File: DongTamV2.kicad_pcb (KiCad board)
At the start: 2 copper layers, 254 parts, among them J1 KF128, J10 USB_C_Receptacle, J11 KF128, J12 KF128, J13 KF128, J14 Screw_Terminal_01x08, J15 Screw_Terminal_01x08, J16 Screw_Terminal_01x08, J17 Screw_Terminal_01x08, J2 KF128, J3 Conn_01x02_Male, J4 Conn_02x03_Odd_Even, J5 Conn_01x05_Male, J6 Conn_01x04_Male, J7 Conn_01x05_Male, J8 Conn_01x05_Male, J9 IDC_02x07, Q1 N_Mosfet, Q10 SI2302, Q11 SI2302, Q12 SI2302, Q13 SI2302, Q14 SI2302, Q15 SI2302, Q16 SI2302, Q17 SI2302, Q18 SI2302, Q19 SI2302, Q2 N_Mosfet, Q20 SI2302, Q21 SI2302, Q3 N_Mosfet, Q4 N_Mosfet, Q5 N_Mosfet, Q6 SI2302, Q7 SI2302, Q8 SI2302, Q9 SI2302, SW1 PTS810, SW2 PTS810, SW3 PTS810, U1 AM22-24W2405V, U10 LD1117, U11 LM324, U12 LM324, U13 LM324, U14 LM324, U15 MCP41010, U16 74HC165, U17 74HC165, U2 SP3485EN, U3 MCU_STM32F103C8Tx, U4 ESP32-WROOM-32, U5 PCF8563TS, U6 AMS5915, U7 74HC595, U8 74HC595, U9 USBLC6-2SC6, Y1 16MHz, Y2 MC-306

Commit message: finish some unconnect pins, draw edge cut board
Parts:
- added H1: MountingHole, MountingHole:MountingHole_3.2mm_M3, F.Cu at (0.00, 0.00)
- added H2: MountingHole, MountingHole:MountingHole_3.2mm_M3, F.Cu at (0.00, 74.5)
- added H3: MountingHole, MountingHole:MountingHole_3.2mm_M3, F.Cu at (246.8, 0.00)
- added H4: MountingHole, MountingHole:MountingHole_3.2mm_M3, F.Cu at (246.8, 74.9)
- added RV2: TC33X_10k, SpiritBoi_Footprint_Library:Potentiometer-Vert-SMD-3P-Bourns_TC33X, F.Cu at (182.8, 44.5)
- D1, D2, D3: value D_TVS -> SMAJ28A
- F1: value Fuse -> 5x20mm 2A
- F2, F3: value Polyfuse -> MF-MSMF050-2
- FL1: value Filter_EMI_LL -> UU9.8-153 15mH
- J14, J15, J16, J17: value Screw_Terminal_01x08 -> KF-5.08-8-V
- Q1, Q2, Q3, Q4, Q5: value N_Mosfet -> SI2302/BSS138
- RV1: value Varistor -> 14D471K
- moved J13 200.1 mm to (10.5, 92.5)
- moved J11 171.2 mm to (39.0, 93.0)
- moved Y1 169.1 mm to (161.5, 5.00)
- moved C10 165.9 mm to (145.2, 12.8)
- moved C11 165.9 mm to (145.2, 15.4)
- moved C12 165.9 mm to (145.2, 18.1)
- moved C9 165.9 mm to (145.2, 10.2)
- moved JP3 165.9 mm to (149.4, 9.75)
- moved LE1 165.9 mm to (153.9, 6.65)
- moved SW1 165.9 mm to (150.7, 14.0)
- moved C5 162.6 mm to (133.0, -9.50)
- moved J12 160.2 mm to (50.0, 92.0)
- moved R10 160.1 mm to (139.5, 16.9)
- moved R11 160.1 mm to (139.5, 19.5)
- moved R12 160.1 mm to (139.5, 22.1)
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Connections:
- R1 pad 1: /RS485/RS485.TX -> /RS485/RS485_input.TX
- R2 pad 1: /RS485/RS485.RX -> /RS485/RS485_input.RX
- U16 pad 1: /ReadValveState/74HC165.LOAD -> /ReadValveState/InputExpanderPort.LOAD
- U16 pad 2: /ReadValveState/74HC165.SCK -> /ReadValveState/InputExpanderPort.SCK
- U16 pad 9: /ReadValveState/74HC165.DATA -> /ReadValveState/InputExpanderPort.DATA
- U17 pad 1: /ReadValveState/74HC165.LOAD -> /ReadValveState/InputExpanderPort.LOAD
- U17 pad 2: /ReadValveState/74HC165.SCK -> /ReadValveState/InputExpanderPort.SCK
- U2 pad 2: /RS485/RS485.DERE -> /RS485/RS485_input.DERE
- U2 pad 3: /RS485/RS485.DERE -> /RS485/RS485_input.DERE
- U3 pad 1: /STM32/VBAT -> +3.3V
- U4 pad 4: /ESP32/BT.s4 -> /ESP32/GUI_Button.s3
- U4 pad 5: /ESP32/BT.s3 -> /ESP32/GUI_Button.s4
- U4 pad 6: /ESP32/BT.s2 -> /ESP32/GUI_Button.s1
- U4 pad 7: /ESP32/BT.s1 -> /ESP32/GUI_Button.s2
- U5 pad 5: /PCF8563/i2c.SDA -> /AMS5915/i2c.SDA
- U5 pad 6: /PCF8563/i2c.SCL -> /AMS5915/i2c.SCL
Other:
- board outline added: 254 x 125.5 mm
- board text added: "Còn Lora, thẻ nhớ, mạch đọc 4-20mA"

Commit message: Add LORA, SDcard and Volt to 4_20mA scheamtic
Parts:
- removed the J5 at (161.0, 12.0)
- removed the J6 at (160.0, 33.5)
- removed JP3, JP4, JP6: SolderJumper_2_Open, Jumper:SolderJumper-2_P1.3mm_Open_RoundedPad1.0x1.5mm
- added C38: 100nF, SpiritBoi_Footprint_Library:C_0603, F.Cu at (82.5, 15.0)
- added C39: 100nF, SpiritBoi_Footprint_Library:C_0603, F.Cu at (-12.4, 37.0)
- added C41: 100nF, SpiritBoi_Footprint_Library:C_0805, F.Cu at (-36.8, 45.3)
- added D25: SMF05C, SpiritBoi_Footprint_Library:Package-IC-TSSOP_6, F.Cu at (74.5, -1.20)
- added D26: SS54, SpiritBoi_Footprint_Library:Package-Diode-D_SMA, F.Cu at (-13.7, 20.0)
- added J17: Micro_SD_Card_Det1, SpiritBoi_Footprint_Library:Socket_MicroSD-9P, F.Cu at (85.2, 8.68)
- added J18: HT3.96mm-3P, SpiritBoi_Footprint_Library:TerminalBlock_bornier-3_P5.08mm, F.Cu at (-23.4, 27.9)
- added J8: ~, SpiritBoi_Footprint_Library:Conn-Vert-THT-2.54mm-2x4P-IDC_Header, F.Cu at (145.5, 25.0)
- added LE19: Blue 0603, SpiritBoi_Footprint_Library:LED_0603, F.Cu at (-12.2, 39.7)
- added LE20: LED 0805, SpiritBoi_Footprint_Library:LED_0805, F.Cu at (-11.9, 34.1)
- added Q22: MMBT3904, SpiritBoi_Footprint_Library:SOT23-3, F.Cu at (-15.6, 15.4)
- added R102: 4k7, SpiritBoi_Footprint_Library:R_0603, F.Cu at (78.3, 15.0)
- added R103: 220R, SpiritBoi_Footprint_Library:R_0603, F.Cu at (-37.0, 14.3)
- added R104: 1k, SpiritBoi_Footprint_Library:R_0603, F.Cu at (-37.0, 16.9)
- added R105: 10k, SpiritBoi_Footprint_Library:R_0603, F.Cu at (-37.0, 19.6)
- added R106: 560R, SpiritBoi_Footprint_Library:R_0603, F.Cu at (-37.0, 22.2)
- added R107: 100k, SpiritBoi_Footprint_Library:R_0603, F.Cu at (-37.0, 24.9)
- added R108: 100k, SpiritBoi_Footprint_Library:R_0603, F.Cu at (-37.0, 27.5)
- added R109: 820k, SpiritBoi_Footprint_Library:R_0603, F.Cu at (-32.9, 14.3)
- added R110: 820k, SpiritBoi_Footprint_Library:R_0603, F.Cu at (-32.9, 16.9)
- added R111: 820k, SpiritBoi_Footprint_Library:R_0603, F.Cu at (-32.9, 19.6)
- added R112: 820k, SpiritBoi_Footprint_Library:R_0603, F.Cu at (-32.9, 22.2)
- added R113: 820k, SpiritBoi_Footprint_Library:R_0603, F.Cu at (-32.9, 24.9)
- added R114: 820k, SpiritBoi_Footprint_Library:R_0603, F.Cu at (-32.9, 27.5)
- added R115: 100R, SpiritBoi_Footprint_Library:R_0603, F.Cu at (-28.8, 14.3)
- added R116: 680k, SpiritBoi_Footprint_Library:R_0603, F.Cu at (-28.8, 16.9)
- added R117: 820k, SpiritBoi_Footprint_Library:R_0603, F.Cu at (-28.8, 19.6)
- added RV3: 100k, SpiritBoi_Footprint_Library:Potentiometer-Vert-THT-Bourns_3296W, F.Cu at (-31.0, 32.1)
- added RV4: 100k, SpiritBoi_Footprint_Library:Potentiometer-Vert-THT-Bourns_3296W, F.Cu at (-31.0, 38.5)
- added U17: RF_Module_Ai-Thinker-Ra-02, SpiritBoi_Footprint_Library:Module-LORA-RA02, F.Cu at (86.0, -15.5)
- added U18: LM324, SpiritBoi_Footprint_Library:Package-IC-Vert-SMD-1.27mm-14P-SOIC_14_Narrow_3.9x8.7mm, F.Cu at (-21.9, 18.3)
- added U19: LM317_TO-252, SpiritBoi_Footprint_Library:Package-IC-Vert-SMD-TO_252_2, F.Cu at (-19.8, 36.5)
- added U20: TL431, SpiritBoi_Footprint_Library:SOT23-3, F.Cu at (-11.3, 15.4)
- J13: renamed from J14; footprint TerminalBlock:TerminalBlock_bornier-8_P5.08mm -> SpiritBoi_Footprint_Library:TerminalBlock-Horz-THT-8P-P5.08mm-KF2EDG_Pluggable
- J14: renamed from J15; footprint TerminalBlock:TerminalBlock_bornier-8_P5.08mm -> SpiritBoi_Footprint_Library:TerminalBlock-Horz-THT-8P-P5.08mm-KF2EDG_Pluggable
- J15: renamed from J16; footprint TerminalBlock:TerminalBlock_bornier-8_P5.08mm -> SpiritBoi_Footprint_Library:TerminalBlock-Horz-THT-8P-P5.08mm-KF2EDG_Pluggable
- J16: renamed from J17; footprint TerminalBlock:TerminalBlock_bornier-8_P5.08mm -> SpiritBoi_Footprint_Library:TerminalBlock-Horz-THT-8P-P5.08mm-KF2EDG_Pluggable
- LE1: value Led -> Blue 0603
- LE10: renamed from LE9; value Blue -> Blue 0603
- LE11: renamed from LE10; value Blue -> Blue 0603
- LE12: renamed from LE11; value Blue -> Blue 0603
- LE13: renamed from LE12; value Blue -> Blue 0603
- LE14: renamed from LE13; value Blue -> Blue 0603
- LE15: renamed from LE14; value Blue -> Blue 0603
- LE16: renamed from LE15; value Blue -> Blue 0603
- LE17: renamed from LE16; value Blue -> Blue 0603
- LE18: renamed from LE17; value Blue -> Blue 0603
- LE2: renamed from LE18; value Led -> Blue 0603
- LE3: renamed from LE2; value Blue -> Blue 0603
- LE4: renamed from LE3; value Blue -> Blue 0603
- LE5: renamed from LE4; value Blue -> Blue 0603
- LE6: renamed from LE5; value Blue -> Blue 0603
- LE7: renamed from LE6; value Blue -> Blue 0603
- LE8: renamed from LE7; value Blue -> Blue 0603
- LE9: renamed from LE8; value Blue -> Blue 0603
- moved J1 251.4 mm to (236.5, -17.5), turned to 180 degrees
- moved C1 250.8 mm to (240.7, -8.24), turned to 180 degrees
- moved RV1 235.4 mm to (239.7, 16.6), turned to 180 degrees
- moved FL1 221.9 mm to (234.1, 25.1), turned to 180 degrees
- moved F1 215.2 mm to (226.0, 3.50), turned to 180 degrees
- moved U1 207.9 mm to (234.8, 63.2), turned to 180 degrees
- moved D1 180.0 mm to (224.9, 79.6)
- moved D2 180.0 mm to (224.9, 84.0)
- moved J2 180.0 mm to (219.0, 92.0)
- moved J3 180.0 mm to (230.0, 91.0)
- moved BTr1 163.6 mm to (43.0, 34.5)
- moved C20 163.6 mm to (56.1, 35.6)
- moved C21 163.6 mm to (56.1, 38.2)
- moved C22 163.6 mm to (56.1, 40.9)
- moved D8 163.6 mm to (52.6, 45.1)
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- renumbered C38 to C36, C36 to C40, D23 to D1, D8 to D10, D9 to D11, D10 to D12, D11 to D13, D12 to D14, D13 to D15, D14 to D16, D15 to D17, D16 to D18, D17 to D19, D24 to D2, D18 to D20, D19 to D21, D20 to D22, D21 to D23, D22 to D24, D5 to D3, D6 to D4, D1 to D5, D2 to D6, D3 to D7, D4 to D8, D7 to D9, H3 to H2, H2 to H3, J13 to J1, J8 to J10, J9 to J11, J10 to J12, J11 to J2, J12 to J3, J1 to J4, J2 to J5, J3 to J6, J4 to J7, J7 to J9, JP7 to JP1, R102 to R118, R103 to R119, R51 to R16, R52 to R17, R53 to R18, R16 to R19, R17 to R20, R18 to R21, R19 to R22, R20 to R23, R21 to R24, R22 to R25, R23 to R26, R24 to R27, R25 to R28, R26 to R29, R27 to R30, R28 to R31, R29 to R32, R30 to R33, R31 to R34, R32 to R35, R33 to R36, R34 to R37, R35 to R38, R36 to R39, R37 to R40, R38 to R41, R39 to R42, R40 to R43, R41 to R44, R42 to R45, R43 to R46, R44 to R47, R45 to R48, R46 to R49, R47 to R50, R48 to R51, R49 to R52, R50 to R53, U17 to U15, U15 to U21
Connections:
- net /STM32/MCP41010.CS renamed /LORA/RA02.CS_MCP41010
- net /STM32/MCP41010.MOSI renamed /LORA/RA02.MOSI
- net /STM32/MCP41010.SCK renamed /LORA/RA02.SCK
- U3 pad 10: Net-(JP4-B) -> /LORA/RA02.CS_LORA
- U3 pad 15: unconnected-(U3-PA5/SPI1_SCK/ADC12_IN5-Pad15) -> /SDcard/DetectCard
- U3 pad 27: Net-(JP3-B) -> /LORA/RA02.MISO
- U3 pad 31: unconnected-(U3-PA10/USART1_RX/TIM1_CH3-Pad31) -> /LORA/RA02.CS_SDcard
- U3 pad 38: Net-(JP6-B) -> unconnected-(U3-PA15/JTDI-Pad38)
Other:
- board text added: "Còn mạch đọc 4-20mA, kiểm tra thứ tự Stlinkv2"
- board text removed: "Còn Lora, thẻ nhớ, mạch đọc 4-20mA"

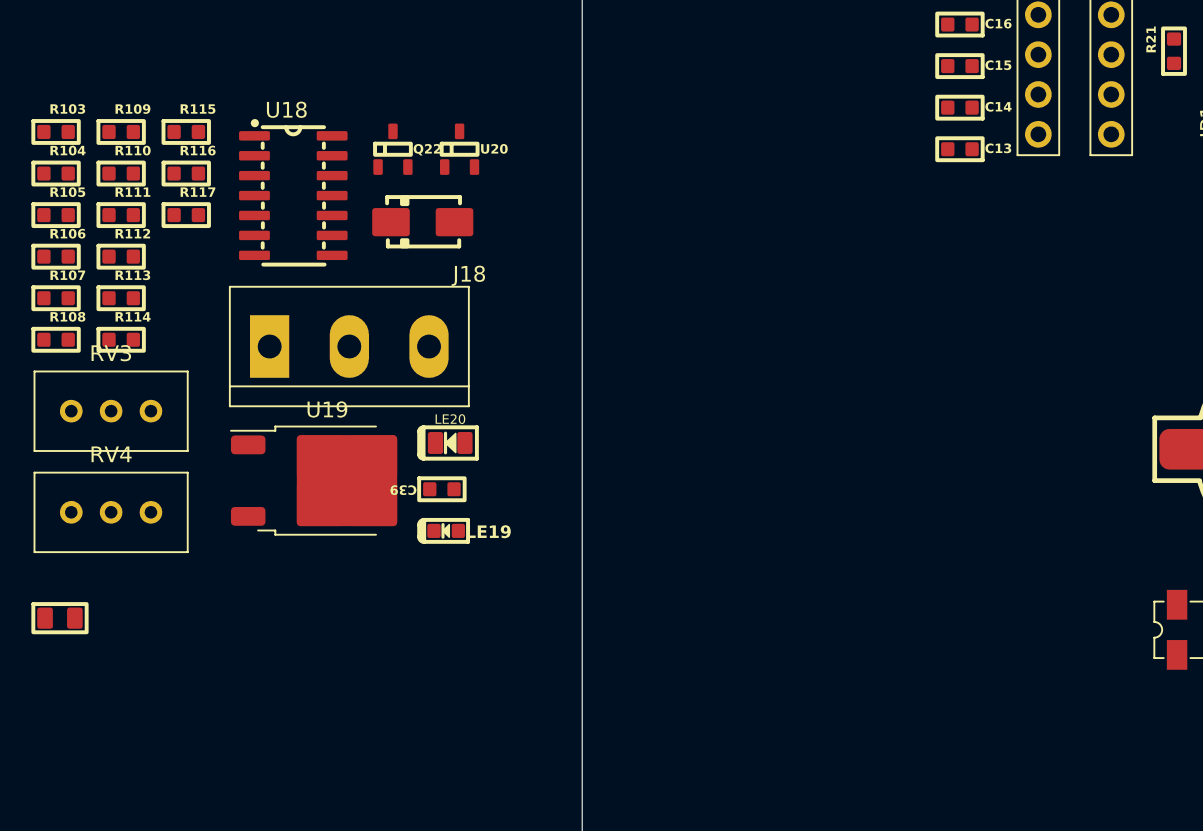
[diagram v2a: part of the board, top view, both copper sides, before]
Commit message: remove old schem files
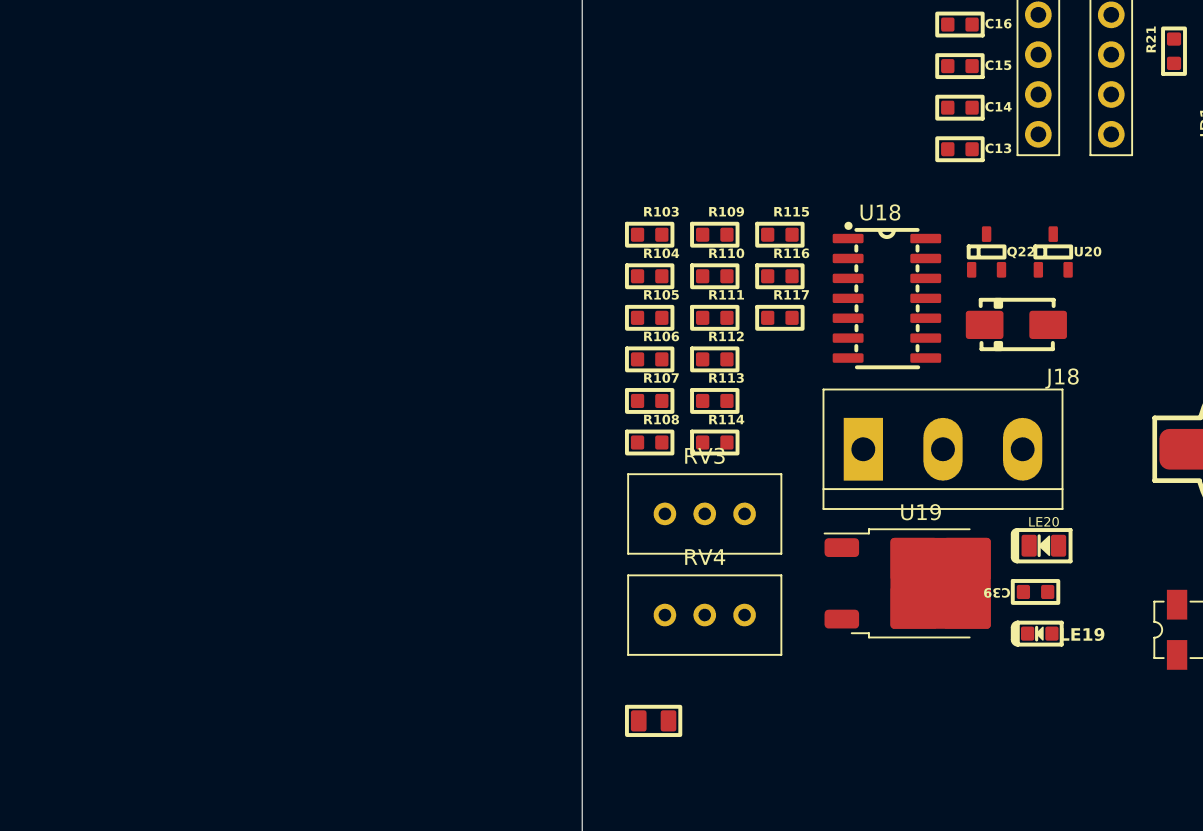
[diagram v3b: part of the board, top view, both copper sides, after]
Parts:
- R17, R18: value 2k2 -> ?
- moved C39 38.4 mm to (25.4, 43.6)
- moved D26 38.4 mm to (24.1, 26.6)
- moved J18 38.4 mm to (14.4, 34.5)
- moved LE19 38.4 mm to (25.7, 46.3)
- moved LE20 38.4 mm to (25.9, 40.6)
- moved Q22 38.4 mm to (22.3, 21.9)
- moved R109 38.4 mm to (4.95, 20.8)
- moved R110 38.4 mm to (4.95, 23.5)
- moved R111 38.4 mm to (4.95, 26.1)
- moved R112 38.4 mm to (4.95, 28.8)
- moved R113 38.4 mm to (4.95, 31.4)
- moved R114 38.4 mm to (4.95, 34.1)
- moved R115 38.4 mm to (9.10, 20.8)
- moved R116 38.4 mm to (9.10, 23.5)
- moved R117 38.4 mm to (9.10, 26.1)
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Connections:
- net Net-(U3-PA9/USART1_TX/TIM1_CH2) renamed /STM32/USB_Detect
- J8 pad 1: /STM32/SWCLK -> +3.3V
- J8 pad 2: /STM32/RX_LOG -> /STM32/5V
- J8 pad 3: /STM32/SWDIO -> GND
- J8 pad 4: /STM32/TX_LOG -> GND
- J8 pad 5: GND -> /STM32/SWDIO
- J8 pad 6: GND -> /STM32/TX_LOG
- J8 pad 7: +3.3V -> /STM32/SWCLK
- J8 pad 8: /STM32/5V -> /STM32/RX_LOG
- U4 pad 10: /ESP32/DAC1 -> /ConverterVoltTo4_20mA/DAC_4_20mA

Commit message: Add README, Lora received interrupt pin
Change LED pin from PB0 to PC13, PCF8563_CLKOUT to PC14
PB0 add Lora received interrupt pin
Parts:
- R13, R16: value 2k2 -> 1k
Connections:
- J8 pad 2: /STM32/5V -> +5V
- R16 pad 1: /PCF8563/CLKOUT -> /STM32/PC14
- U17 pad 5: unconnected-(U17-DIO0-Pad5) -> /LORA/LoRaReceivedInterrupt
- U3 pad 14: /PCF8563/CLKOUT -> /SDcard/DetectCard
- U3 pad 15: /SDcard/DetectCard -> /STM32/595.SRCLK
- U3 pad 16: /STM32/595.SRCLK -> /STM32/595.RCLK
- U3 pad 18: /STM32/595.RCLK -> /LORA/LoRaReceivedInterrupt
- U3 pad 19: /STM32/LED -> /STM32/4_20mA
- U3 pad 2: /STM32/PC13 -> /STM32/LED
- U5 pad 7: /PCF8563/CLKOUT -> /STM32/PC14
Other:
- board text added: "Còn mạch đọc 4-20mA"
- board text removed: "Còn mạch đọc 4-20mA, kiểm tra thứ tự Stlinkv2"

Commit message: Feat: Components's layout
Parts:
- moved C41 241.2 mm to (242.0, 40.2), turned to 90 degrees
- moved U17 177.6 mm to (253.2, 44.2)
- moved LE6 118.3 mm to (42.0, 140.6), turned to 0 degrees
- moved R28 118.1 mm to (45.6, 140.6), turned to 180 degrees
- moved C36 114.1 mm to (151.8, 116.8)
- moved U15 113.5 mm to (158.3, 118.8)
- moved R26 107.5 mm to (55.9, 140.6), turned to 180 degrees
- moved LE4 107.2 mm to (52.2, 140.6), turned to 0 degrees
- moved R27 103.3 mm to (65.9, 140.8), turned to 180 degrees
- moved R116 102.9 mm to (49.0, 118.3)
- moved LE5 102.7 mm to (62.2, 140.8), turned to 0 degrees
- moved R115 102.2 mm to (45.6, 116.3)
- moved U6 99.3 mm to (181.8, 43.8)
- moved R117 99.1 mm to (45.5, 118.3), turned to 180 degrees
- moved C1 99.1 mm to (256.9, 89.5)
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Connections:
- J1 pad 1: /DualPowerSupply-220V-to-24V_5V_AM22/220V_L -> /DualPowerSupply-220V-to-24V_5V_AM22/220V_N
- J1 pad 2: /DualPowerSupply-220V-to-24V_5V_AM22/220V_N -> /DualPowerSupply-220V-to-24V_5V_AM22/220V_L
- J5 pad 1: /RS485/B_RS485 -> /RS485/Earth
- J5 pad 3: /RS485/Earth -> /RS485/B_RS485
- Y2 pad 1: Net-(U5-OSCO) -> Net-(U5-OSCI)
- Y2 pad 4: Net-(U5-OSCI) -> Net-(U5-OSCO)
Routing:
- net GND: track 0.00 -> 358.5 mm, vias 0 -> 2
- net +5V: track 0.00 -> 171.3 mm
- net +3V3: track 0.00 -> 117.7 mm
- net Net-(C1-Pad2): track 0.00 -> 83.1 mm
- net /ESP32/RST: track 0.00 -> 65.7 mm
- net /GUI_IDC_Header/IC74595.SER: track 0.00 -> 61.9 mm
- net /GUI_IDC_Header/IC74595.SRCLK: track 0.00 -> 51.5 mm, vias 0 -> 1
- net /GUI_IDC_Header/LCD_I2C_LOGIC_SCL: track 0.00 -> 46.9 mm, vias 0 -> 2
- net /GUI_IDC_Header/LCD_I2C_LOGIDC_SDA: track 0.00 -> 46.7 mm
- net /GUI_IDC_Header/IC74595.RCLK: track 0.00 -> 43.7 mm, vias 0 -> 1
- net /RS485/A1_RS485: track 0.00 -> 43.0 mm
- net +3.3V: track 0.00 -> 41.5 mm, vias 0 -> 1
- net /DualPowerSupply-220V-to-24V_5V_AM22/220V_N: track 0.00 -> 41.1 mm
- net Net-(U1-L): track 0.00 -> 39.4 mm
- net /ESP32/GUI_Button.s4: track 0.00 -> 36.8 mm, vias 0 -> 1
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
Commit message: fix board dimension and add module HW685
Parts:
- added REF**: Module-Current_To_Volt-HW_685, SpiritBoi_Footprint_Library:Module-Current_To_Volt-HW_685, F.Cu at (152.7, 39.0)
- moved C28 21.1 mm to (205.9, 104.3)
- moved C29 21.1 mm to (203.2, 104.3)
- moved C30 21.1 mm to (191.2, 107.3)
- moved C31 21.1 mm to (188.2, 107.3)
- moved D3 21.1 mm to (197.6, 111.5)
- moved D4 21.1 mm to (197.8, 100.5)
- moved U10 21.1 mm to (196.9, 106.2)
- moved C10 15.2 mm to (170.9, 96.5)
- moved C11 15.2 mm to (166.0, 106.0)
- moved C12 15.2 mm to (156.3, 102.8)
- moved C6 15.2 mm to (153.3, 95.5)
- moved C7 15.2 mm to (159.6, 90.8)
- moved C8 15.2 mm to (153.3, 102.0)
- moved C9 15.2 mm to (159.6, 92.5)
- moved J7 15.2 mm to (159.6, 86.0)
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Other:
- board size 254 x 125.5 mm -> 254.1 x 135.1 mm

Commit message: Fix & Update: ESP32 and STM32 layout
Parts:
- moved U17 191.6 mm to (80.4, 118.8), turned to 90 degrees
- moved C41 191.5 mm to (76.4, 130.1), turned to 180 degrees
- moved REF** 97.4 mm to (222.9, 106.6), turned to 0 degrees
- moved U6 74.1 mm to (152.9, 105.2), turned to 180 degrees
- moved LE7 68.7 mm to (152.4, 153.5)
- moved R29 68.7 mm to (156.1, 153.5)
- moved R82 68.0 mm to (193.3, 156.1)
- moved R19 62.9 mm to (135.6, 89.0), turned to 90 degrees
- moved SW2 59.4 mm to (131.2, 69.2)
- moved C18 57.2 mm to (132.9, 66.4), turned to 0 degrees
- moved R20 56.1 mm to (129.5, 66.4)
- moved C23 56.0 mm to (155.4, 95.7), turned to 180 degrees
- moved C36 55.4 mm to (202.1, 139.9), turned to 180 degrees
- moved R119 53.9 mm to (134.6, 51.8), turned to 180 degrees
- moved J10 52.3 mm to (120.0, 37.4), turned to 0 degrees
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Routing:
- net +24V: track 9.46 -> 429.3 mm
- net GND: track 358.5 -> 226.8 mm
- net +3V3: track 117.7 -> 16.9 mm
- net +5V: track 171.3 -> 101.7 mm
- net /GUI_IDC_Header/IC74595.SER: track 61.9 -> 0.00 mm
- net /ESP32/RST: track 65.7 -> 13.0 mm
- net /GUI_IDC_Header/IC74595.SRCLK: track 51.5 -> 0.00 mm, vias 1 -> 0
- net /GUI_IDC_Header/LCD_I2C_LOGIC_SCL: track 46.9 -> 0.00 mm, vias 2 -> 0
- net /GUI_IDC_Header/LCD_I2C_LOGIDC_SDA: track 46.7 -> 0.00 mm
- net /GUI_IDC_Header/IC74595.RCLK: track 43.7 -> 0.00 mm, vias 1 -> 0
- net /ESP32/GUI_Button.s4: track 36.8 -> 0.00 mm, vias 1 -> 0
- net /STM32/PC14: track 0.00 -> 36.2 mm
- net /ESP32/GUI_Button.s3: track 34.9 -> 0.00 mm, vias 1 -> 0
- net /STM32/TX_LOG: track 0.00 -> 31.8 mm
- net /ESP32/GUI_Button.s1: track 31.2 -> 0.00 mm, vias 1 -> 0
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- added copper zone on F.Cu, net +24V
- added copper zone on F.Cu, net +5V
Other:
- board size 254.1 x 135.1 mm -> 203 x 135 mm

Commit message: fix: Size of board and position of components
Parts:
- moved REF** 137.3 mm to (114.9, 21.8), turned to -90 degrees
- moved R102 112.2 mm to (32.1, 58.2), turned to -90 degrees
- moved J17 111.4 mm to (25.9, 69.0), turned to -90 degrees
- moved D25 109.4 mm to (34.6, 58.2), turned to 90 degrees
- moved C38 106.5 mm to (37.1, 58.4), turned to -90 degrees
- moved R119 94.9 mm to (40.9, 66.9), turned to -90 degrees
- moved U21 90.6 mm to (44.7, 66.9), turned to -90 degrees
- moved J18 90.3 mm to (141.2, 25.5), turned to 180 degrees
- moved R118 86.8 mm to (44.4, 71.9), turned to 180 degrees
- moved C40 86.5 mm to (48.4, 66.9), turned to 90 degrees
- moved RV2 84.1 mm to (44.4, 75.4), turned to 90 degrees
- moved RV3 80.8 mm to (147.3, 32.9), turned to 90 degrees
- moved LE20 80.7 mm to (123.4, 34.0), turned to -90 degrees
- moved R108 79.1 mm to (143.6, 33.6), turned to -90 degrees
- moved D26 78.9 mm to (126.5, 34.5), turned to 90 degrees
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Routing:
- net (no net): track 0.00 -> 433.1 mm
- net +24V: track 429.3 -> 67.8 mm
- net GND: track 226.8 -> 142.1 mm, vias 2 -> 0
- net /GUI_IDC_Header/IC74595.OE: track 0.00 -> 36.4 mm, vias 0 -> 1
- net /ESP32/VSPI.CLK: track 0.00 -> 32.2 mm, vias 0 -> 2
- net /ESP32/GUI_Button.s4: track 0.00 -> 32.2 mm, vias 0 -> 1
- net /ESP32/GUI_Button.s3: track 0.00 -> 31.9 mm, vias 0 -> 1
- net /ESP32/ESP32_I2C.SDA: track 0.00 -> 29.2 mm, vias 0 -> 2
- net /ESP32/VSPI.MOSI: track 0.00 -> 28.3 mm, vias 0 -> 2
- net /ESP32/ESP32_I2C.SCL: track 0.00 -> 28.3 mm, vias 0 -> 2
- net /ESP32/GUI_Button.s2: track 0.00 -> 28.0 mm, vias 0 -> 1
- net /ESP32/GUI_Button.s1: track 0.00 -> 27.2 mm, vias 0 -> 1
- net /GUI_IDC_Header/LCD_I2C_LOGIDC_SDA: track 0.00 -> 25.5 mm
- net /ESP32/VSPI.CS0: track 0.00 -> 25.3 mm, vias 0 -> 2
- net /ESP32/RST: track 13.0 -> 36.0 mm, vias 0 -> 1
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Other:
- board size 203 x 135 mm -> 254 x 135 mm
